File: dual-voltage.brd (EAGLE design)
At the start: 25.3 x 25.4 mm, 14 parts

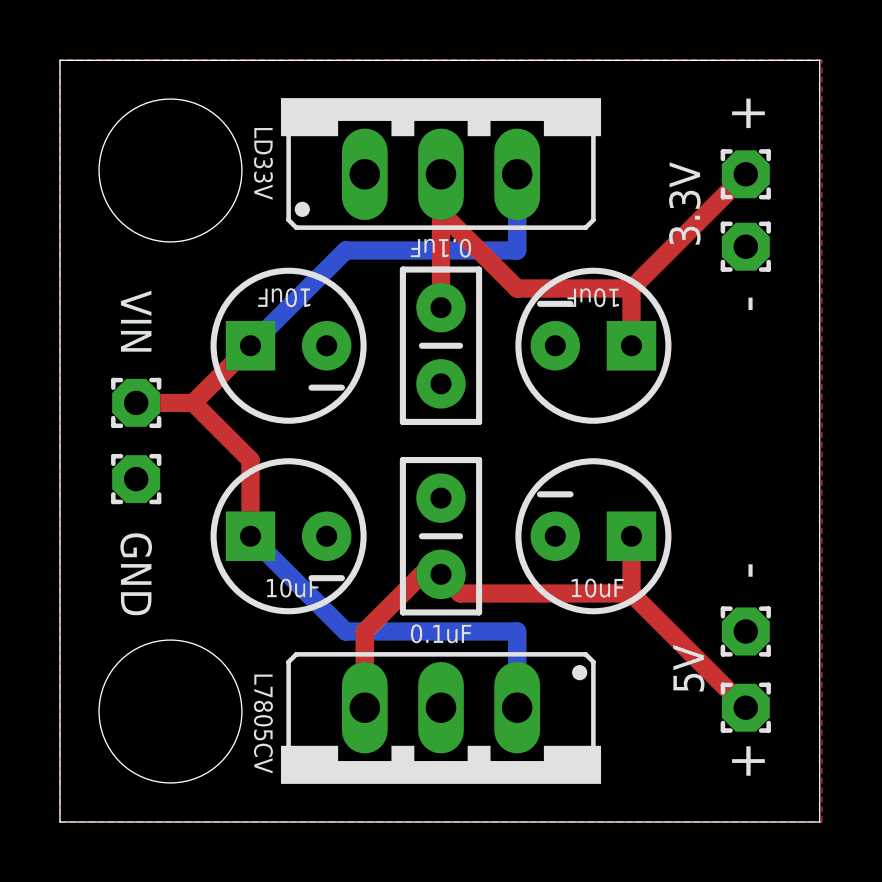
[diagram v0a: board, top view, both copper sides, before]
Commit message: Trace updates for new 3.3v regulator
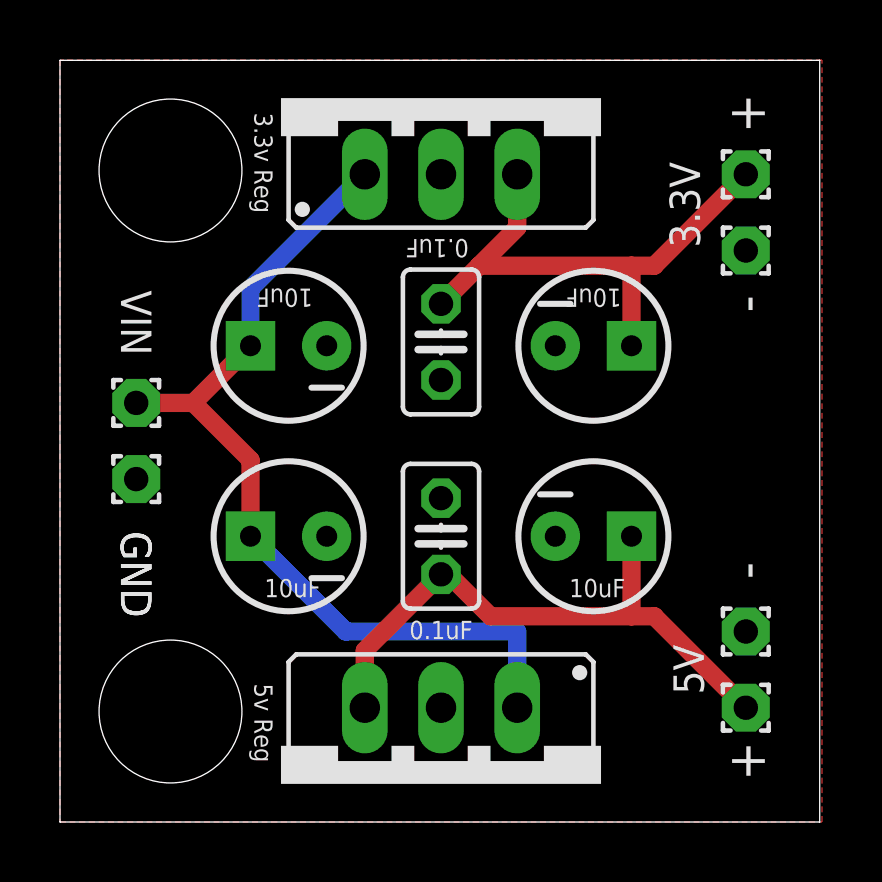
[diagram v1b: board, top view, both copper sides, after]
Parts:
- removed C3, C6: 0.1uF, SparkFun-Capacitors:CAP-PTH-SMALLEZ
- removed LD33V: (no value), v-reg:317TS
- added 3.3VREG: (no value), v-reg:78XXS
- added C7: (no value), rcl:C025-025X050
- added C8: 0.1uF, rcl:C025-025X050
- moved 3.3VGND 0.13 mm to (22.9, 19.1)
- renumbered L7805C to 5VREG
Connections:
- net 3.3V: now also 3.3VREG.OUT, C7.1; no longer C6.1, LD33V.2
- net 5V: now also C8.1; no longer C3.1
- net GND: now also 3.3VREG.GND, C7.2, C8.2; no longer C3.2, C6.2, LD33V.1
- net N$1: now also 3.3VREG.IN; no longer LD33V.3
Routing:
- net N$1: track 35.3 -> 29.9 mm
- net 3.3V: track 19.1 -> 18.2 mm
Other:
- board text added: "0.1uF"
- board text added: "3.3v Reg"
- board text added: "5v Reg"
- board text added: "http://git.io/dualvolt"
- board text removed: "L7805CV"
- board text removed: "LD33V"
- board text removed: "http://git.io/camtech1"

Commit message: Updates voltage in/out jumpers to SparkFun components, updates 0.1uF capacitor footprint to SparkFun, bumps version to 1.1.0
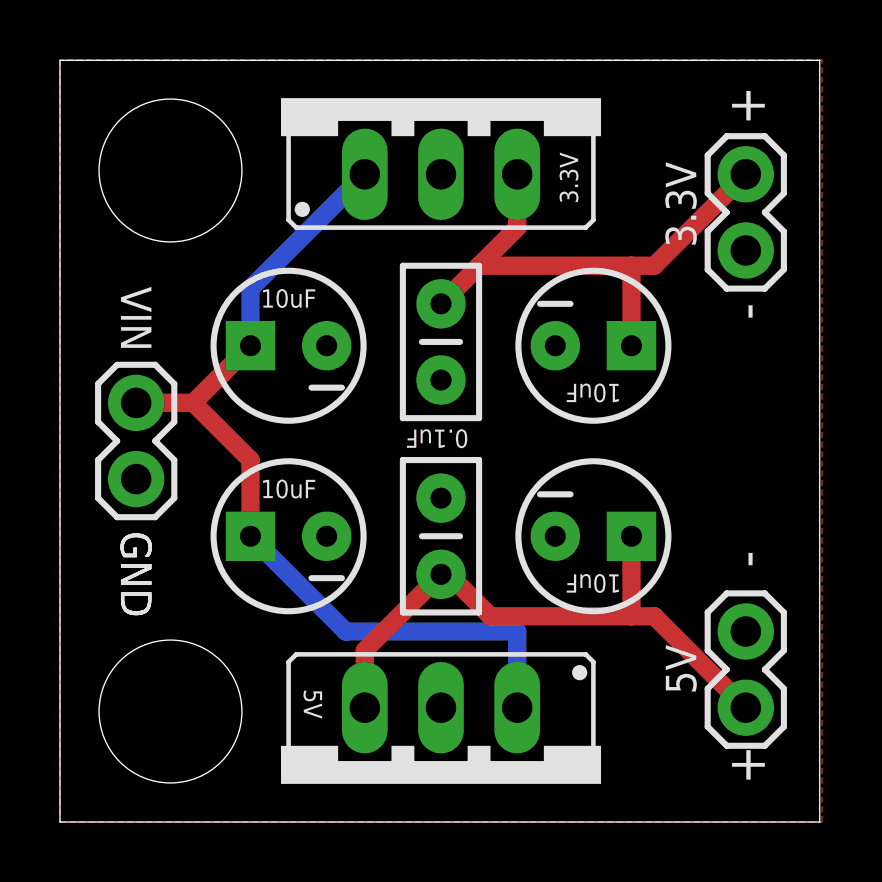
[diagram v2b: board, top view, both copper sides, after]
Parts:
- removed 3.3V, 5V: (no value), wirepad:1,6/0,8
- removed 3.3VGND, 5VGND, VINGND: GND, wirepad:1,6/0,8
- removed V1: VIN, wirepad:1,6/0,8
- added 3.3VOUT, 5VOUT, VIN: (no value), SparkFun-Passives:1X02
- C7, C8: device rcl:C025-025X050 -> SparkFun-Passives:CAP-PTH-SMALL2
- moved C7 1.27 mm to (12.7, 17.3)
- moved C8 1.27 mm to (12.7, 8.26)
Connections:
- net 3.3V: now also 3.3VOUT.1; no longer 3.3V.1
- net 5V: now also 5VOUT.1; no longer 5V.1
- net GND: now also 3.3VOUT.2, 5VOUT.2, VIN.2; no longer 3.3VGND.1, 5VGND.1, VINGND.1
- net N$1: now also VIN.1; no longer V1.1
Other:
- board text added: "CT533"
- board text added: "v1.1.0"
- board text removed: "3.3v Reg"
- board text removed: "5v Reg"
- board text removed: "v1.0.0"
